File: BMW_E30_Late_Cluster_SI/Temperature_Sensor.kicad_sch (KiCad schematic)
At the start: 31 parts, among them Q11 BC327-16, Q12 BC337-25, Q13 BC337-16, Q14 BC547B, Q15 BC557B, Q17 BC337-25

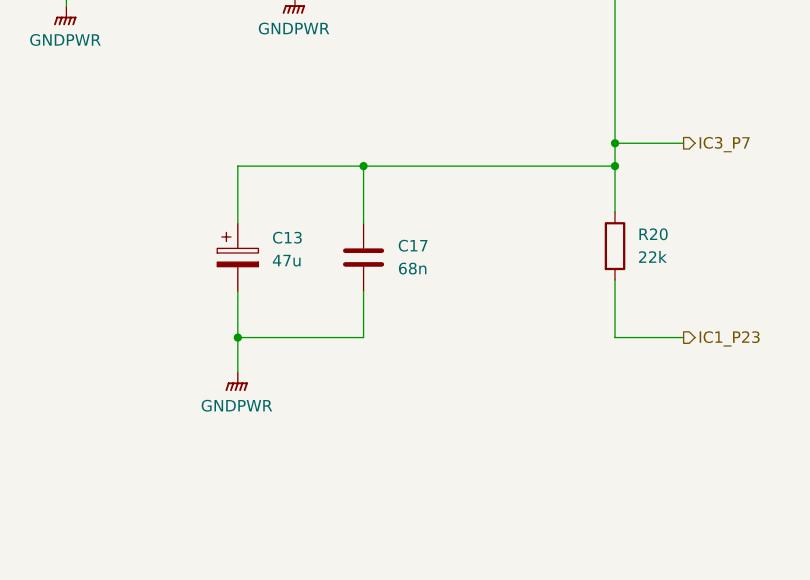
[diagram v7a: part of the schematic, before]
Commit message: Moved C17 for readability
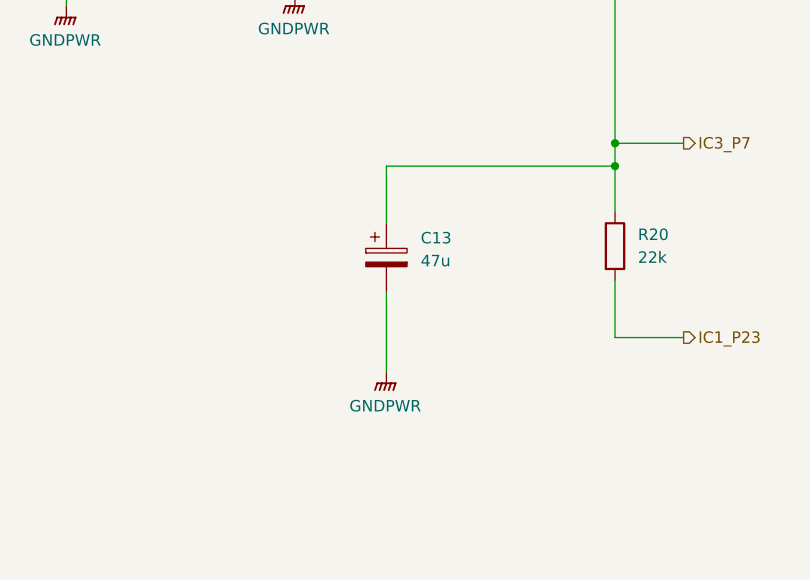
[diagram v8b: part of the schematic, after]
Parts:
- removed C17: 68n, Capacitor_THT:C_Disc_D6.0mm_W2.5mm_P5.00mm, symbol Device:C
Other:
- moved on the sheet: C13
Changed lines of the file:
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@@
 	)
 	(junction
-		(at 215.9 118.11)
-		(diameter 0)
-		(color 0 0 0 0)
-	)
-	(junction
 		(at 162.56 62.23)
 		(diameter 0)
@@
 	)
 	(junction
-		(at 201.93 137.16)
-		(diameter 0)
-		(color 0 0 0 0)
-	)
-	(junction
 		(at 116.84 106.68)
 		(diameter 0)
@@
 	(wire
 		(pts
-			(xy 201.93 137.16) (xy 215.9 137.16)
-		)
-		(stroke
-			(width 0)
-			(type default)
-		)
-	)
-	(wire
-		(pts
 			(xy 101.6 168.91) (xy 109.22 168.91)
 		)
@@
 	(wire
 		(pts
-			(xy 201.93 137.16) (xy 201.93 140.97)
+			(xy 218.44 132.08) (xy 218.44 140.97)
 		)
 		(stroke
@@
 	(wire
 		(pts
-			(xy 201.93 124.46) (xy 201.93 118.11)
+			(xy 218.44 124.46) (xy 218.44 118.11)
 		)
 		(stroke
@@
 	(wire
 		(pts
-			(xy 215.9 118.11) (xy 243.84 118.11)
-		)
-		(stroke
-			(width 0)
-			(type default)
-		)
-	)
-	(wire
-		(pts
 			(xy 243.84 66.04) (xy 266.7 66.04)
 		)
@@
 	(wire
 		(pts
-			(xy 215.9 124.46) (xy 215.9 118.11)
-		)
-		(stroke
-			(width 0)
-			(type default)
-		)
-	)
-	(wire
-		(pts
 			(xy 123.19 57.15) (xy 128.27 57.15)
 		)
@@
 	(wire
 		(pts
-			(xy 215.9 132.08) (xy 215.9 137.16)
-		)
-		(stroke
-			(width 0)
-			(type default)
-		)
-	)
-	(wire
-		(pts
 			(xy 111.76 57.15) (xy 106.68 57.15)
 		)
@@
 	(wire
 		(pts
-			(xy 201.93 118.11) (xy 215.9 118.11)
+			(xy 218.44 118.11) (xy 243.84 118.11)
 		)
 		(stroke
@@
 		)
 	)
-	(wire
-		(pts
-			(xy 201.93 132.08) (xy 201.93 137.16)
-		)
-		(stroke
-			(width 0)
-			(type default)
-		)
-	)
 	(hierarchical_label "IC1_P19"
 		(shape output)
@@
 	(symbol
 		(lib_id "Device:C_Polarized")
-		(at 201.93 128.27 0)
+		(at 218.44 128.27 0)
 		(unit 1)
 		(exclude_from_sim no)
@@
 		(fields_autoplaced yes)
 		(property "Reference" "C13"
-			(at 205.74 126.1109 0)
+			(at 222.25 126.1109 0)
 			(effects
 				(font
@@
 		)
 		(property "Value" "47u"
-			(at 205.74 128.6509 0)
+			(at 222.25 128.6509 0)
 			(effects
 				(font
@@
 		)
 		(property "Footprint" "Capacitor_THT:CP_Radial_Tantal_D9.0mm_P2.50mm"
-			(at 202.8952 132.08 0)
+			(at 219.4052 132.08 0)
 			(effects
 				(font
@@
 		)
 		(property "Datasheet" "~"
-			(at 201.93 128.27 0)
+			(at 218.44 128.27 0)
 			(effects
 				(font
@@
 		)
 		(property "Description" "16v"
-			(at 201.93 128.27 0)
+			(at 218.44 128.27 0)
 			(effects
 				(font
@@
 		)
 		(property "Vendor Link" ""
-			(at 201.93 128.27 0)
+			(at 218.44 128.27 0)
 			(effects
 				(font
@@
 	)
 	(symbol
-		(lib_id "Device:C")
-		(at 215.9 128.27 0)
-		(unit 1)
-		(exclude_from_sim no)
-		(in_bom yes)
-		(on_board yes)
-		(dnp no)
-		(fields_autoplaced yes)
-		(property "Reference" "C17"
-			(at 219.71 126.9999 0)
-			(effects
-				(font
-					(size 1.27 1.27)
-				)
-				(justify left)
-			)
-		)
-		(property "Value" "68n"
-			(at 219.71 129.5399 0)
-			(effects
-				(font
-					(size 1.27 1.27)
-				)
-				(justify left)
-			)
-		)
-		(property "Footprint" "Capacitor_THT:C_Disc_D6.0mm_W2.5mm_P5.00mm"
-			(at 216.8652 132.08 0)
-			(effects
-				(font
-					(size 1.27 1.27)
-				)
-				(hide yes)
-			)
-		)
-		(property "Datasheet" "~"
-			(at 215.9 128.27 0)
-			(effects
-				(font
-					(size 1.27 1.27)
-				)
-				(hide yes)
-			)
-		)
-		(property "Description" "Unpolarized capacitor"
-			(at 215.9 128.27 0)
-			(effects
-				(font
-					(size 1.27 1.27)
-				)
-				(hide yes)
-			)
-		)
-		(property "Vendor Link" ""
-			(at 215.9 128.27 0)
-			(effects
-				(font
-					(size 1.27 1.27)
-				)
-				(hide yes)
-			)
-		)
-		(pin "2"
-		)
-		(pin "1"
-		)
-		(instances
-			(project "BMW_E30_Late_Cluster_SI"
-				(path "/00d578f4-1582-4e4e-9a07-e5462d38fb61/84ca9cc6-3e51-42c7-8f6d-11ef7495b962"
-					(reference "C17")
-					(unit 1)
-				)
-			)
-		)
-	)
-	(symbol
 		(lib_id "Device:R")
 		(at 81.28 53.34 0)
@@
 	(symbol
 		(lib_id "power:GNDPWR")
-		(at 201.93 140.97 0)
+		(at 218.44 140.97 0)
 		(unit 1)
 		(exclude_from_sim no)
@@
 		(fields_autoplaced yes)
 		(property "Reference" "#PWR018"
-			(at 201.93 146.05 0)
+			(at 218.44 146.05 0)
 			(effects
 				(font
@@
 		)
 		(property "Value" "GNDPWR"
-			(at 201.803 144.78 0)
+			(at 218.313 144.78 0)
 			(effects
 				(font
@@
 		)
 		(property "Footprint" ""
-			(at 201.93 142.24 0)
+			(at 218.44 142.24 0)
 			(effects
 				(font
@@
 		)
 		(property "Datasheet" ""
-			(at 201.93 142.24 0)
+			(at 218.44 142.24 0)
 			(effects
 				(font
@@
 		)
 		(property "Description" "Power symbol creates a global label with name \"GNDPWR\" , global ground"
-			(at 201.93 140.97 0)
+			(at 218.44 140.97 0)
 			(effects
 				(font
